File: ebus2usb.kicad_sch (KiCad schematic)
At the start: 38 parts, among them J1 MKDSN1,5/2-5,08, J2 Molex 53047-0210, J3 Molex 53047-0410, J4 Molex 53047-0210, J5 Molex 53047-0410, J6 Molex 67068-8000, Q1 BC817-40, Q2 BC817-40, U1 TS3702, U2 ADuM1201, U3 CH340N

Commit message: v0.8.1 * Size of main board changed to 87mm x 14.8mm * R5 changed from 1K5 to 4K7 * TS3702/TCL3702 replaced by TSX3702 (need VCC on one input)
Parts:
- R5: value 1K5 -> 4K7; LCSC C4310 -> C17673; Part UNI-ROYAL(Uniroyal Elec) 0805W8F1501T5E -> UNI-ROYAL(Uniroyal Elec) 0805W8F4701T5E
- U1: value TS3702 -> TSX3702; LCSC C283319 -> C2970396; Part STMicroelectronics TS3702CDT -> STMicroelectronics TSX3702IDT
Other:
- note removed: "[Alternatives] TS3702: TLC3702"
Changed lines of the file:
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@@
   (title_block
     (title "eBUS to USB Adapter")
-    (date "2023-05-07")
-    (rev "v0.8")
+    (date "2023-05-15")
+    (rev "v0.8.1")
     (company "(c) 2023 by jkyprian")
   )
@@
   (text "Reference Voltage for Comparators" (at 171.45 24.13 0)
     (effects (font (size 1.27 1.27)) (justify left bottom))
-  )
-  (text "[Alternatives] TS3702: TLC3702\n" (at 101.6 149.225 0)
-    (effects (font (size 1.27 1.27) (color 132 132 132 1)) (justify left bottom))
   )
   (text "Power from eBus" (at 82.55 24.13 0)
@@
       (effects (font (size 1.27 1.27)) (justify left) hide)
     )
-    (property "Value" "TS3702" (at 83.82 120.65 0)
+    (property "Value" "TSX3702" (at 83.82 120.65 0)
       (effects (font (size 1.27 1.27)) hide)
     )
@@
       (effects (font (size 1.27 1.27)) hide)
     )
-    (property "Datasheet" "https://www.st.com/resource/en/datasheet/ts3702.pdf" (at 83.82 120.65 0)
-      (effects (font (size 1.27 1.27)) hide)
-    )
-    (property "LCSC" "C283319" (at 83.82 120.65 0)
-      (effects (font (size 1.27 1.27)) hide)
-    )
-    (property "Part" "STMicroelectronics TS3702CDT" (at 83.82 120.65 0)
+    (property "Datasheet" "https://www.st.com/resource/en/datasheet/tsx3702.pdf" (at 83.82 120.65 0)
+      (effects (font (size 1.27 1.27)) hide)
+    )
+    (property "LCSC" "C2970396" (at 83.82 120.65 0)
+      (effects (font (size 1.27 1.27)) hide)
+    )
+    (property "Part" "STMicroelectronics TSX3702IDT" (at 83.82 120.65 0)
       (effects (font (size 1.27 1.27)) hide)
     )
@@
       (effects (font (size 1.27 1.27)))
     )
-    (property "Value" "TS3702" (at 73.66 115.57 0)
+    (property "Value" "TSX3702" (at 73.66 115.57 0)
       (effects (font (size 1.27 1.27)))
     )
@@
       (effects (font (size 1.27 1.27)) hide)
     )
-    (property "Datasheet" "https://www.st.com/resource/en/datasheet/ts3702.pdf" (at 78.74 120.65 0)
-      (effects (font (size 1.27 1.27)) hide)
-    )
-    (property "LCSC" "C283319" (at 78.74 120.65 0)
-      (effects (font (size 1.27 1.27)) hide)
-    )
-    (property "Part" "STMicroelectronics TS3702CDT" (at 78.74 120.65 0)
+    (property "Datasheet" "https://www.st.com/resource/en/datasheet/tsx3702.pdf" (at 78.74 120.65 0)
+      (effects (font (size 1.27 1.27)) hide)
+    )
+    (property "LCSC" "C2970396" (at 78.74 120.65 0)
+      (effects (font (size 1.27 1.27)) hide)
+    )
+    (property "Part" "STMicroelectronics TSX3702IDT" (at 78.74 120.65 0)
       (effects (font (size 1.27 1.27)) hide)
     )
@@
       (effects (font (size 1.27 1.27)))
     )
-    (property "Value" "1K5" (at 63.5 116.84 90)
+    (property "Value" "4K7" (at 63.5 116.84 90)
       (effects (font (size 1.27 1.27)))
     )
@@
       (effects (font (size 1.27 1.27)) hide)
     )
-    (property "LCSC" "C4310" (at 63.5 120.65 0)
-      (effects (font (size 1.27 1.27)) hide)
-    )
-    (property "Part" "UNI-ROYAL(Uniroyal Elec) 0805W8F1501T5E" (at 63.5 120.65 0)
+    (property "LCSC" "C17673" (at 63.5 120.65 0)
+      (effects (font (size 1.27 1.27)) hide)
+    )
+    (property "Part" "UNI-ROYAL(Uniroyal Elec) 0805W8F4701T5E" (at 63.5 120.65 0)
       (effects (font (size 1.27 1.27)) hide)
     )
@@
       (effects (font (size 1.27 1.27)))
     )
-    (property "Value" "TS3702" (at 138.43 115.57 0)
+    (property "Value" "TSX3702" (at 138.43 115.57 0)
       (effects (font (size 1.27 1.27)))
     )
@@
       (effects (font (size 1.27 1.27)) hide)
     )
-    (property "Datasheet" "https://www.st.com/resource/en/datasheet/ts3702.pdf" (at 134.62 120.65 0)
-      (effects (font (size 1.27 1.27)) hide)
-    )
-    (property "LCSC" "C283319" (at 134.62 120.65 0)
-      (effects (font (size 1.27 1.27)) hide)
-    )
-    (property "Part" "STMicroelectronics TS3702CDT" (at 134.62 120.65 0)
-      (effects (font (size 1.27 1.27)) hide)
-    )
+    (property "Datasheet" "https://www.st.com/resource/en/datasheet/tsx3702.pdf" (at 134.62 120.65 0)
+      (effects (font (size 1.27 1.27)) hide)
+    )
+    (property "LCSC" "C2970396" (at 134.62 120.65 0)
+      (effects (font (size 1.27 1.27)) hide)
+    )
+    (property "Part" "STMicroelectronics TSX3702IDT" (at 134.62 120.65 0)
+      (effects (font (size 1.27 1.27)) hide)
+    )

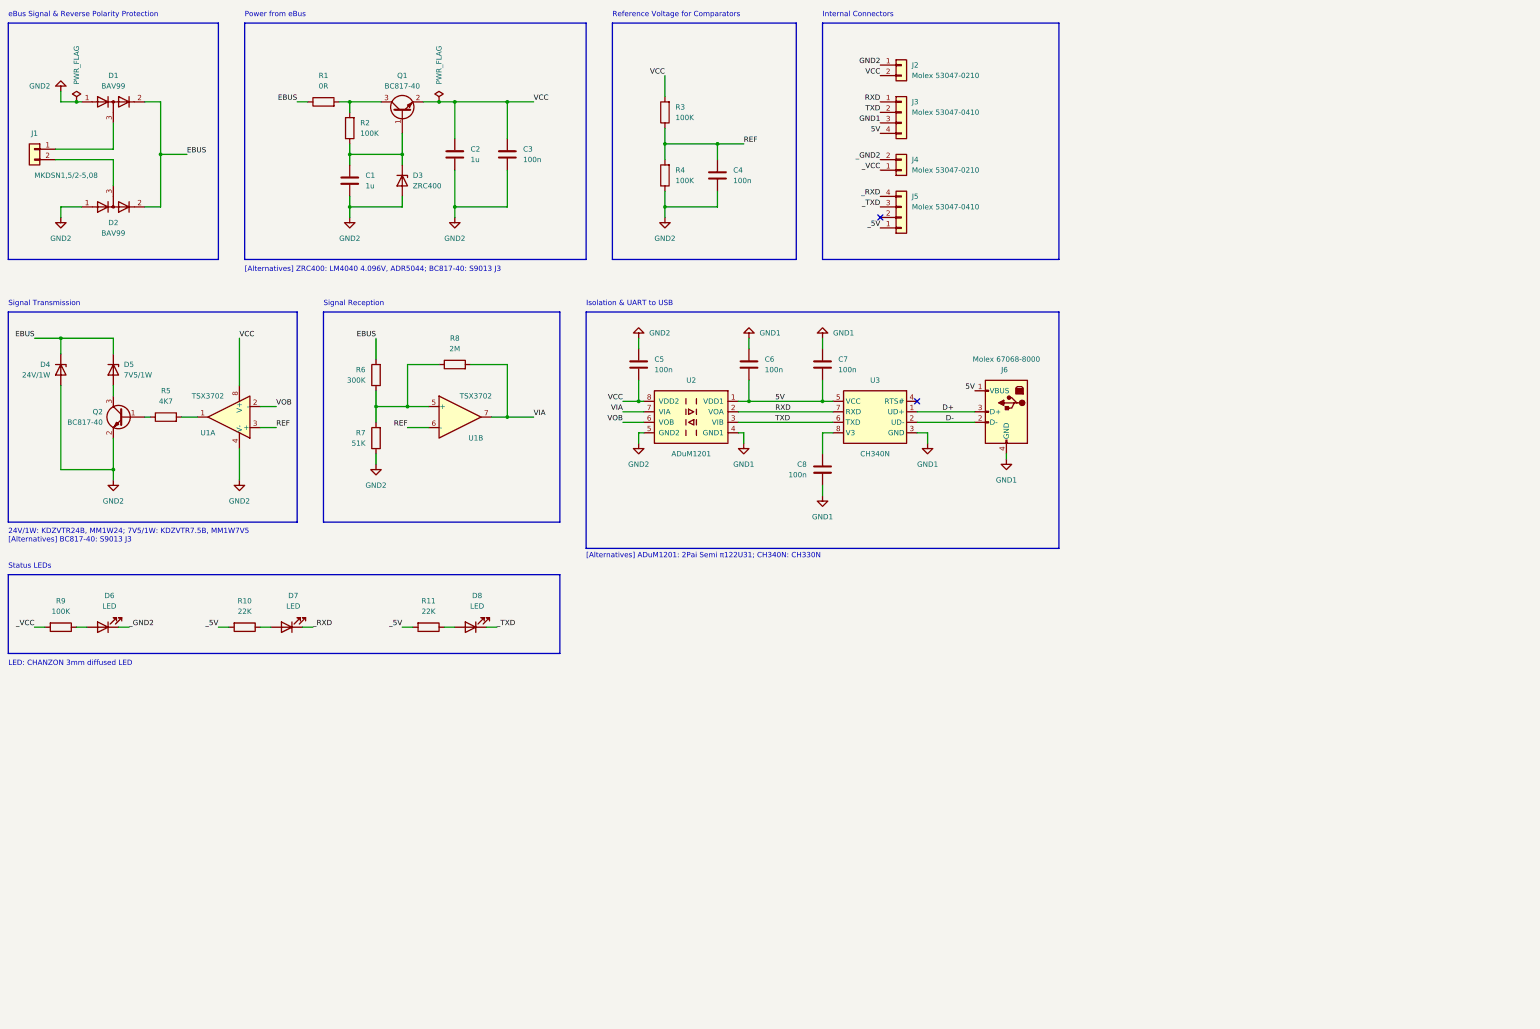
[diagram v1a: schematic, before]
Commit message: * Replaced voltage reference with low IZT 5V6 zener diode (cheaper but increases power consumption on the eBus side by ~200uA) * C2/C4 changed to 10u * R6/R7 adjusted for ~5V VCC * AZV3002 as replacement for TSX3702 * USB Type-B port replaced by Type-C port * ESC protection for USB port * Phoenix Contact MKDSN connector replaced by MSTBA
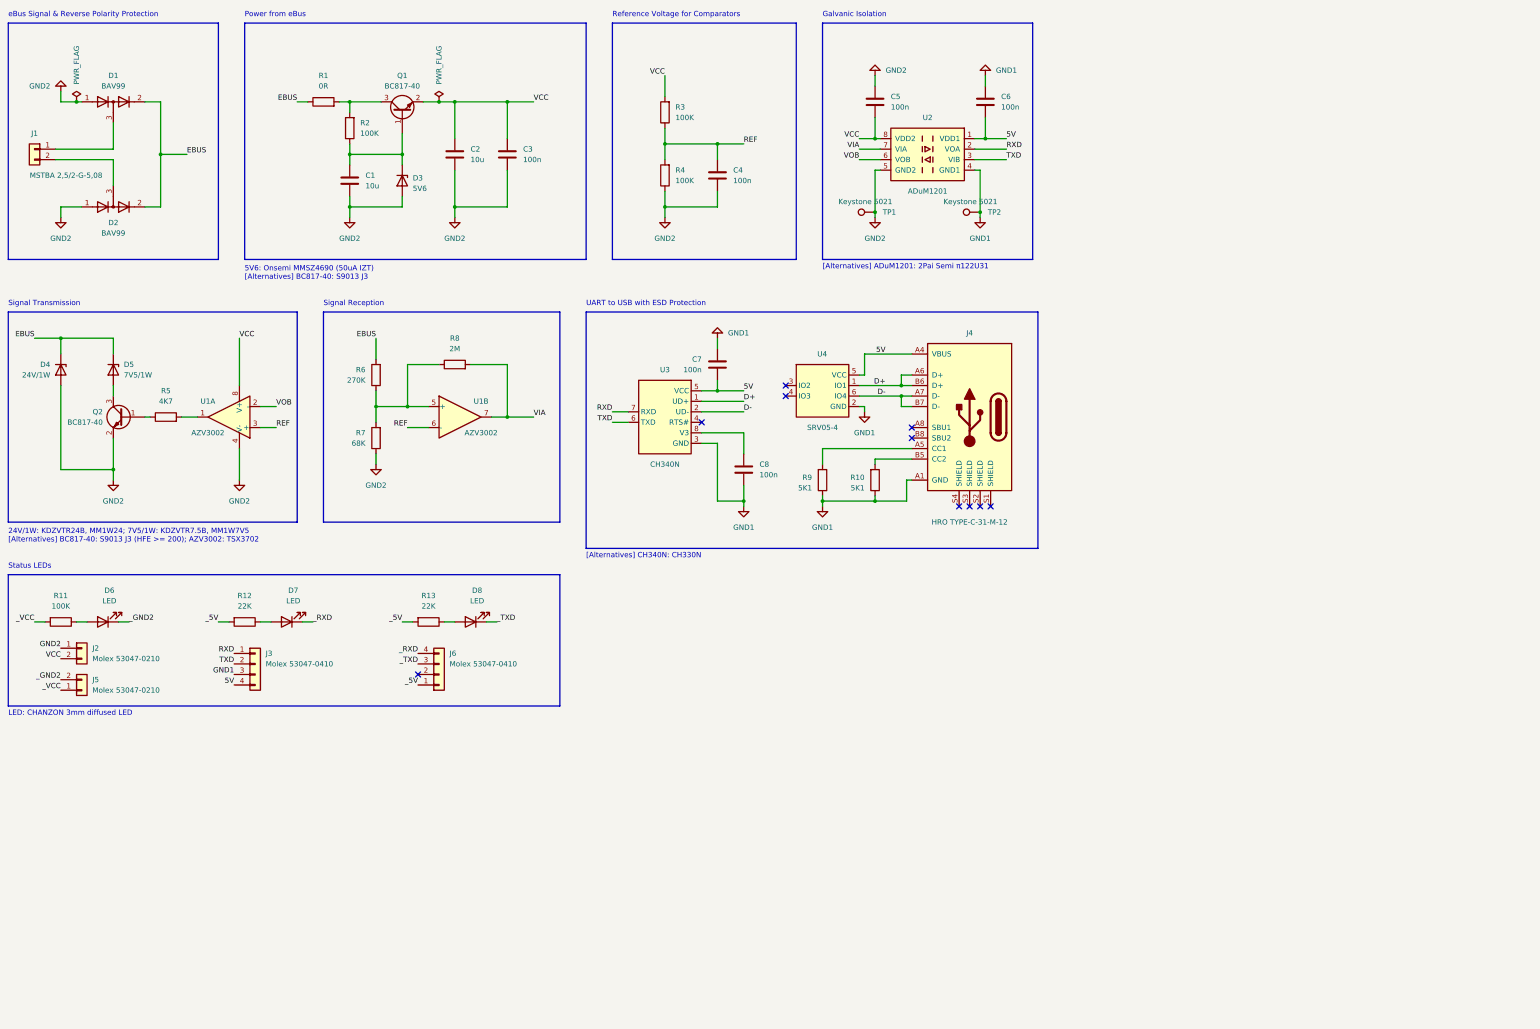
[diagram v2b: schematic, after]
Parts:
- removed J6: Molex 67068-8000, ebus2usb:Molex_670688000, symbol ebus2usb:USB_B
- added J4: HRO TYPE-C-31-M-12, ebus2usb:HRO_TYPE-C-31-M-12, symbol ebus2usb:USB_C
- added R10, R9: 5K1, ebus2usb:R0805, symbol Device:R
- added TP1, TP2: Keystone 5021, ebus2usb:Keystone_5021, symbol Connector:TestPoint
- added U4: SRV05-4, ebus2usb:SOT-23-6L, symbol ebus2usb:SRV05-4
- C1, C2: value 1u -> 10u; LCSC C28323 -> C15850; Part Samsung Electro-Mechanics CL21B105KBFNNNE -> Samsung Electro-Mechanics CL21A106KAYNNNE
- D3: value ZRC400 -> 5V6; footprint ebus2usb:SOT-23-3 -> ebus2usb:SOD-123; LCSC C2156870 -> C152307; Part Diodes Incorporated ZRC400F01TA -> Onsemi MMSZ4690T3G
- D7, D8: Part CHANZON 3mm Diffused LED -> CHANZON 3mm diffused LED
- J1: value MKDSN1,5/2-5,08 -> MSTBA 2,5/2-G-5,08; footprint ebus2usb:MKDSN1,5_2-5,08 -> ebus2usb:MSTBA_2,5_2-G-5,08; LCSC C91153 -> C3697; Part Phoenix Contact MKDSN 1,5/ 2-5,08 -> Phoenix Contact MSTBA 2,5/ 2-G-5,08
- Q1, Q2: LCSC C52801 -> C6749
- R6: value 300K -> 270K; LCSC C17616 -> C17589; Part UNI-ROYAL(Uniroyal Elec) 0805W8F3003T5E -> UNI-ROYAL(Uniroyal Elec) 0805W8F2703T5E
- R7: value 51K -> 68K; LCSC C17737 -> C17801; Part UNI-ROYAL(Uniroyal Elec) 0805W8F5102T5E -> UNI-ROYAL(Uniroyal Elec) 0805W8F6802T5E
- U1: value TSX3702 -> AZV3002; LCSC C2970396 -> C5123396; Part STMicroelectronics TSX3702IDT -> Diodes Incorporated AZV3002S-13
- renumbered J4 to J5, J5 to J6, R9 to R11, R10 to R12, R11 to R13
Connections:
- net 5V: now also J4.A4 (VBUS), J4.A9 (VBUS), J4.B4 (VBUS), J4.B9 (VBUS), U4.5 (VCC)
- net D+: now also J4.A6 (D+), J4.B6 (D+), U4.1 (IO1)
- net D-: now also J4.A7 (D-), J4.B7 (D-), U4.6 (IO4)
- net GND1: now also J4.A1 (GND), J4.A12 (GND), J4.B1 (GND), J4.B12 (GND), R10.1, R9.1, TP2.1, U4.2 (GND)
- net GND2: now also TP1.1
- new net: J4.B5 (CC2), R10.2
- new net: J4.A5 (CC1), R9.2
- no-connect marks 2 -> 10
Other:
- note added: "24V/1W: KDZVTR24B, MM1W24; 7V5/1W: KDZVTR7.5B, MM1W7V5 [Alternatives] BC817-40: S9013 J3 (HFE >= 200); AZV3002: TSX3702"
- note added: "5V6: Onsemi MMSZ4690 (50uA IZT) [Alternatives] BC817-40: S9013 J3"
- note added: "Galvanic Isolation"
- note added: "UART to USB with ESD Protection"
- note added: "[Alternatives] ADuM1201: 2Pai Semi π122U31"
- note added: "[Alternatives] CH340N: CH330N"
- note removed: "24V/1W: KDZVTR24B, MM1W24; 7V5/1W: KDZVTR7.5B, MM1W7V5 [Alternatives] BC817-40: S9013 J3"
- note removed: "Internal Connectors"
- note removed: "Isolation & UART to USB"
- note removed: "[Alternatives] ADuM1201: 2Pai Semi π122U31; CH340N: CH330N"
- note removed: "[Alternatives] ZRC400: LM4040 4.096V, ADR5044; BC817-40: S9013 J3"
- moved on the sheet: C5, C6, C7, C8, D6, D7, D8, J2, J3, J5, J6, R11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

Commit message: New version with STM32 microcontroller.
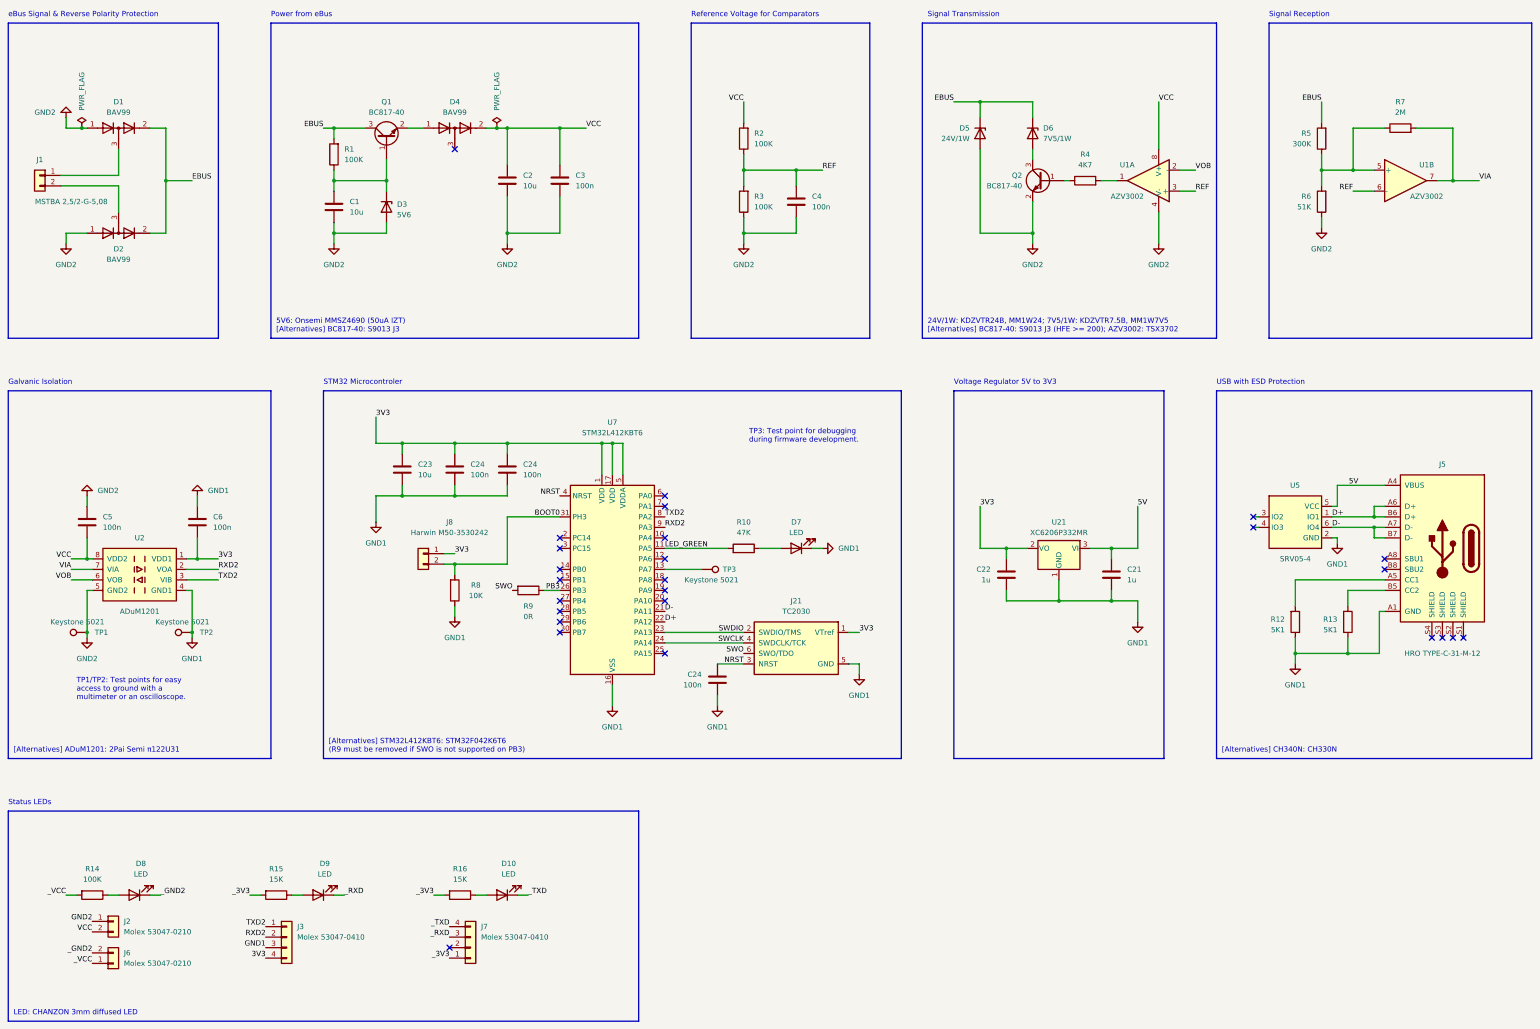
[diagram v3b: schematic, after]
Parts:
- removed C7, C8: 100n, ebus2usb:C0805, symbol Device:C
- removed R1: 0R, ebus2usb:R0805, symbol Device:R
- removed U3: CH340N, ebus2usb:SO08, symbol ebus2usb:CH330N
- added C21, C22: 1u, ebus2usb:C0805, symbol Device:C
- added C23: 10u, ebus2usb:C0805, symbol Device:C
- added C24 (x3): 100n, ebus2usb:C0603, symbol Device:C
- added D4: BAV99, ebus2usb:SOT-23-3, symbol Diode:BAV99
- added D7: LED, ebus2usb:LED_0603, symbol Device:LED
- added J21: TC2030, ebus2usb:TC-2030NL, symbol ebus2usb:TC2030
- added J8: Harwin M50-3530242, ebus2usb:PinHeader_1x02_P1.27mm, symbol Connector_Generic:Conn_01x02
- added R10: 47K, ebus2usb:R0603, symbol Device:R
- added R8: 10K, ebus2usb:R0603, symbol Device:R
- added R9: 0R, ebus2usb:R0603, symbol Device:R
- added TP3: Keystone 5021, ebus2usb:Keystone_5021, symbol Connector:TestPoint
- added U21: XC6206P332MR, ebus2usb:SOT-23-3, symbol Regulator_Linear:XC6206PxxxMR
- added U7: STM32L412KBT6, ebus2usb:LQFP-32, symbol MCU_ST_STM32L4:STM32L412KBTx
- C3, C4, C5, C6: footprint ebus2usb:C0805 -> ebus2usb:C0603; LCSC C28233 -> C14663; Part Samsung Electro-Mechanics CL21B104KCFNNNE -> YAGEO CC0603KRX7R9BB104
- R1: renamed from R2; footprint ebus2usb:R0805 -> ebus2usb:R0603; LCSC C149504 -> C25803; Part UNI-ROYAL(Uniroyal Elec) 0805W8F1003T5E -> UNI-ROYAL(Uniroyal Elec) 0603WAF1003T5E
- R12: renamed from R9; footprint ebus2usb:R0805 -> ebus2usb:R0603; LCSC C27834 -> C23186; Part UNI-ROYAL(Uniroyal Elec) 0805W8F5101T5E -> UNI-ROYAL(Uniroyal Elec) 0603WAF5101T5E
- R13: renamed from R10; footprint ebus2usb:R0805 -> ebus2usb:R0603; LCSC C27834 -> C23186; Part UNI-ROYAL(Uniroyal Elec) 0805W8F5101T5E -> UNI-ROYAL(Uniroyal Elec) 0603WAF5101T5E
- R15: renamed from R12; value 22K -> 15K; LCSC C17560 -> C17475; Part UNI-ROYAL(Uniroyal Elec) 0805W8F2202T5E -> UNI-ROYAL(Uniroyal Elec) 0805W8F1502T5E
- R16: renamed from R13; value 22K -> 15K; LCSC C17560 -> C17475; Part UNI-ROYAL(Uniroyal Elec) 0805W8F2202T5E -> UNI-ROYAL(Uniroyal Elec) 0805W8F1502T5E
- R2: renamed from R3; footprint ebus2usb:R0805 -> ebus2usb:R0603; LCSC C149504 -> C25803; Part UNI-ROYAL(Uniroyal Elec) 0805W8F1003T5E -> UNI-ROYAL(Uniroyal Elec) 0603WAF1003T5E
- R3: renamed from R4; footprint ebus2usb:R0805 -> ebus2usb:R0603; LCSC C149504 -> C25803; Part UNI-ROYAL(Uniroyal Elec) 0805W8F1003T5E -> UNI-ROYAL(Uniroyal Elec) 0603WAF1003T5E
- R4: renamed from R5; footprint ebus2usb:R0805 -> ebus2usb:R0603; LCSC C17673 -> C23162; Part UNI-ROYAL(Uniroyal Elec) 0805W8F4701T5E -> UNI-ROYAL(Uniroyal Elec) 0603WAF4701T5E
- R5: renamed from R6; value 270K -> 300K; footprint ebus2usb:R0805 -> ebus2usb:R0603; LCSC C17589 -> C23024; Part UNI-ROYAL(Uniroyal Elec) 0805W8F2703T5E -> UNI-ROYAL(Uniroyal Elec) 0603WAF3003T5E
- R6: renamed from R7; value 68K -> 51K; footprint ebus2usb:R0805 -> ebus2usb:R0603; LCSC C17801 -> C23196; Part UNI-ROYAL(Uniroyal Elec) 0805W8F6802T5E -> UNI-ROYAL(Uniroyal Elec) 0603WAF5102T5E
- R7: renamed from R8; footprint ebus2usb:R0805 -> ebus2usb:R0603; LCSC C26112 -> C22976; Part UNI-ROYAL(Uniroyal Elec) 0805W8F2004T5E -> UNI-ROYAL(Uniroyal Elec) 0603WAF2004T5E
- renumbered D8 to D10, D4 to D5, D5 to D6, D6 to D8, D7 to D9, J4 to J5, J5 to J6, J6 to J7, R11 to R14, U4 to U5
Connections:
- net 5V: now also C21.1, U21.3 (VI); no longer C6.2, J3.4 (Pin_4), U2.1 (VDD1)
- net D+: now also U7.22 (PA12)
- net D-: now also U7.21 (PA11)
- net EBUS: now also Q1.3 (C), R1.2
- net GND1: now also C21.2, C22.2, C23.2, C24.2, C24.2, C24.2, D7.1 (K), J21.5 (GND), R8.1, U21.1 (GND), U7.16 (VSS), U7.32 (VSS)
- net VCC: now also D4.2 (A); no longer Q1.2 (E)
- net _RXD: now also J7.3 (Pin_3); no longer J7.4 (Pin_4)
- net _TXD: now also J7.4 (Pin_4); no longer J7.3 (Pin_3)
- net RXD renamed RXD2
- net RXD2: now also J3.2 (Pin_2), U7.9 (PA3); no longer J3.1 (Pin_1)
- net TXD renamed TXD2
- net TXD2: now also J3.1 (Pin_1), U7.8 (PA2); no longer J3.2 (Pin_2)
- net _5V renamed _3V3
- new net: D7.2 (A), R10.1
- new net: D4.1 (K), Q1.2 (E)
- new net: TP3.1, U7.13 (PA7)
- new net 3V3: C22.1, C23.1, C24.1, C24.1, C6.2, J21.1 (VTref), J3.4 (Pin_4), J8.1 (Pin_1), U2.1 (VDD1), U21.2 (VO), U7.1 (VDD), U7.17 (VDD), U7.5 (VDDA)
- new net BOOT0: J8.2 (Pin_2), R8.2, U7.31 (PH3)
- new net LED_GREEN: R10.2, U7.11 (PA5)
- new net NRST: C24.1, J21.3 (NRST), U7.4 (NRST)
- new net PB3: R9.1, U7.26 (PB3)
- new net SWCLK: J21.4 (SWDCLK/TCK), U7.24 (PA14)
- new net SWDIO: J21.2 (SWDIO/TMS), U7.23 (PA13)
- new net SWO: J21.6 (SWO/TDO), R9.2
- no-connect marks 10 -> 26
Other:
- note added: "STM32 Microcontroler"
- note added: "TP1/TP2: Test points for easy access to ground with a multimeter or an oscilloscope."
- note added: "TP3: Test point for debugging during firmware development."
- note added: "USB with ESD Protection"
- note added: "Voltage Regulator 5V to 3V3"
- note added: "[Alternatives] STM32L412KBT6: STM32F042K6T6 (R9 must be removed if SWO is not supported on PB3)"
- note removed: "UART to USB with ESD Protection"
- moved on the sheet: C1, C2, C3, C4, C5, C6, D1, D10, D2, D3, D5, D6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
